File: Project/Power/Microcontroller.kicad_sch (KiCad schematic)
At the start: 11 parts, among them J13 I2C, J14 SWD, J15 SPI1, SW1 SW_Push, U14 STM32L422KBTx

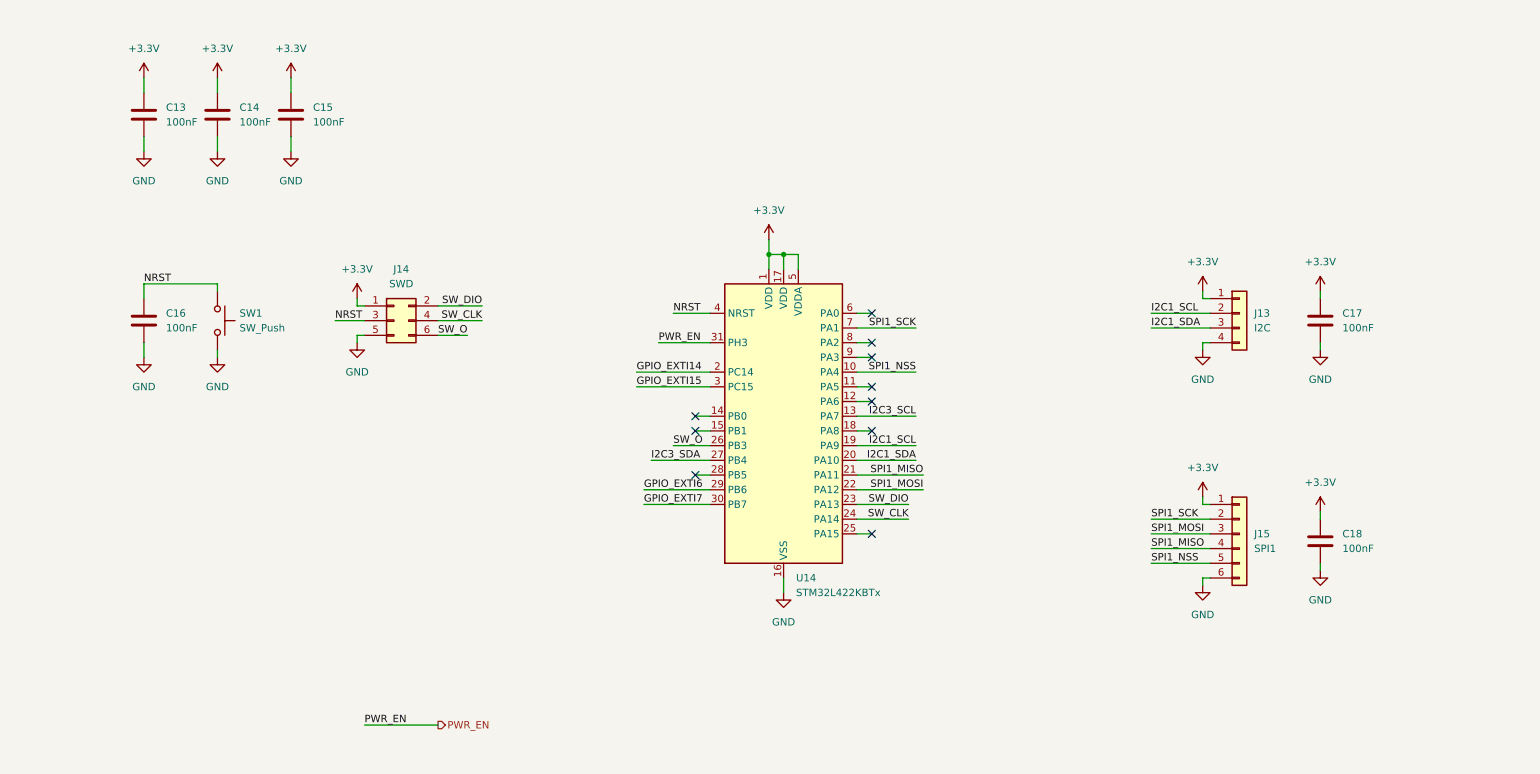
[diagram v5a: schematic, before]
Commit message: Change power microcontroller pin ordering
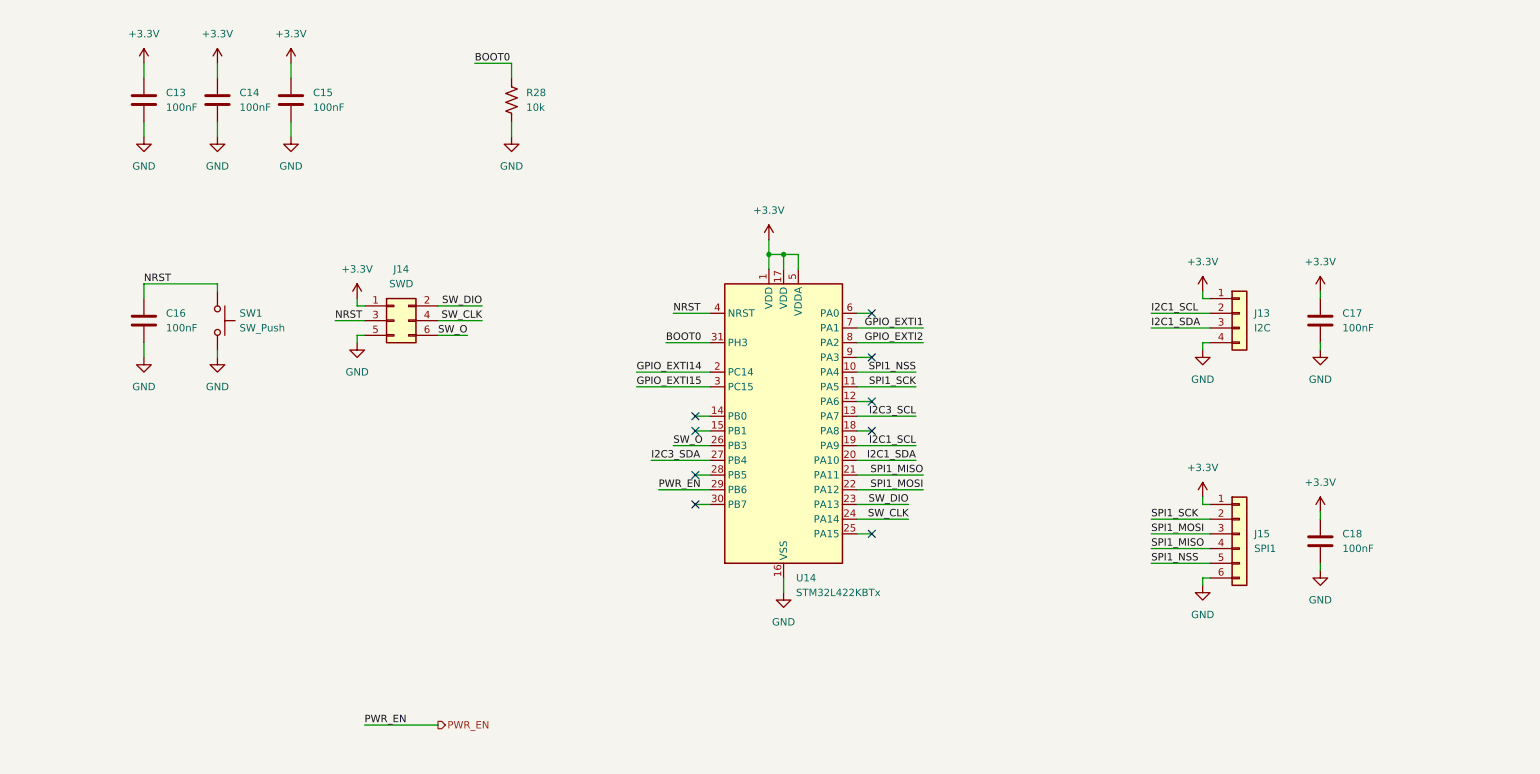
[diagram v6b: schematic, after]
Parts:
- added R28: 10k, Resistor_SMD:R_0603_1608Metric, symbol Device:R_US
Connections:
- net GPIO_EXTI6 is gone; now on net PWR_EN: U14.29 (PB6)
- net GND: now also R28.1
- net PWR_EN: no longer U14.31 (PH3)
- net SPI1_SCK: now also U14.11 (PA5); no longer U14.7 (PA1)
- net GPIO_EXTI2: now reaches U14.8 (PA2)
- net GPIO_EXTI7: no longer names the net of U14.30 (PB7)
- new net BOOT0: R28.2, U14.31 (PH3)
- new net GPIO_EXTI1: U14.7 (PA1)
- no-connect marks 10 -> 9
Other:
- moved on the sheet: C13, C14, C15

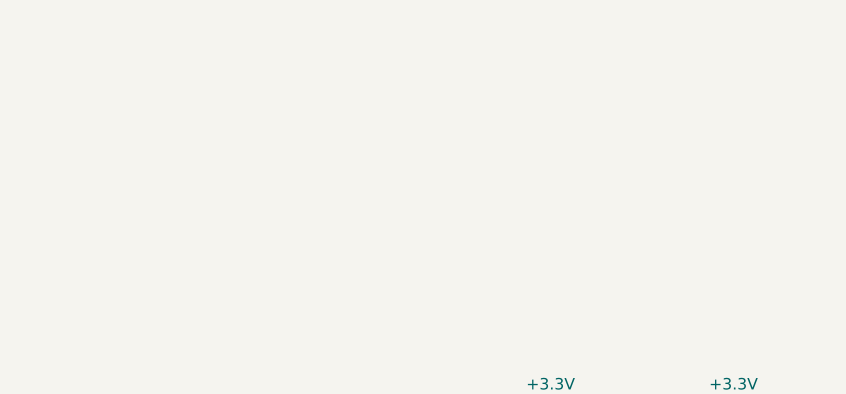
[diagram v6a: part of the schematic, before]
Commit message: Add I2C pull-up resistors
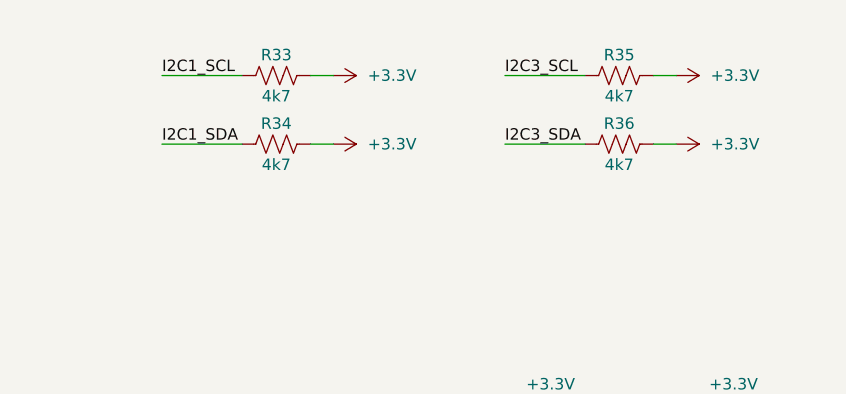
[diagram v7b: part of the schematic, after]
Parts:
- added R33, R34, R35, R36: 4k7, Resistor_SMD:R_0603_1608Metric, symbol Device:R_US
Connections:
- net +3.3V: now also R33.1, R34.1, R35.1, R36.1
- net I2C1_SCL: now also R33.2
- net I2C1_SDA: now also R34.2
- net I2C3_SCL: now also R35.2
- net I2C3_SDA: now also R36.2

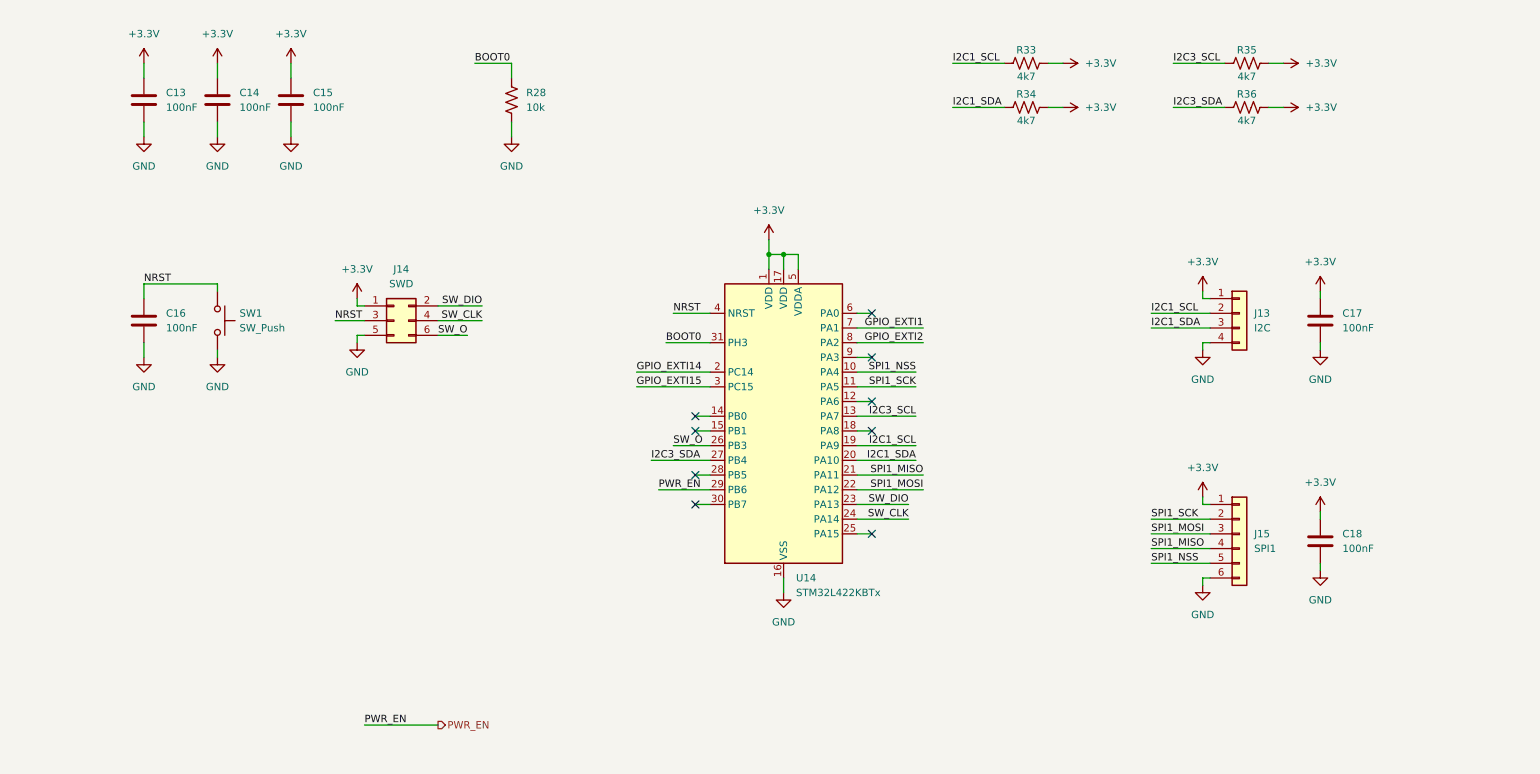
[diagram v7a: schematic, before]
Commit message: Add INA226 sensors for batteries
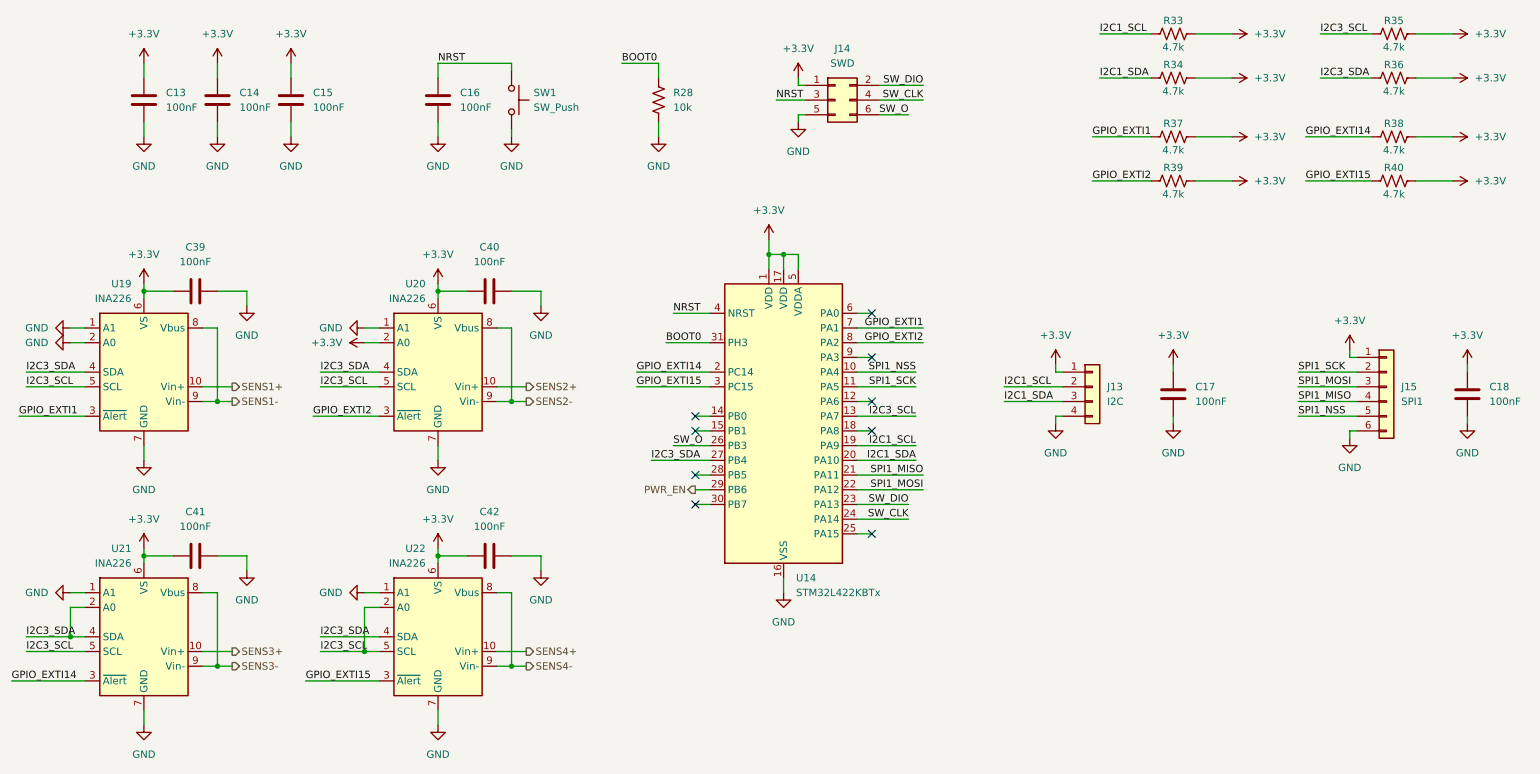
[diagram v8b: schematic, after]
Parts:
- added C39, C40, C41, C42: 100nF, Capacitor_SMD:C_0603_1608Metric, symbol Device:C
- added R37, R38, R39, R40: 4.7k, Resistor_SMD:R_0603_1608Metric, symbol Device:R_US
- added U19, U20, U21, U22: INA226, Package_SO:VSSOP-10_3x3mm_P0.5mm, symbol Sensor_Energy:INA226
- R33, R34, R35, R36: value 4k7 -> 4.7k
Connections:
- net +3.3V: now also C39.1, C40.1, C41.1, C42.1, R37.1, R38.1, R39.1, R40.1, U19.6 (VS), U20.2 (A0), U20.6 (VS), U21.6 (VS), U22.6 (VS)
- net GND: now also C39.2, C40.2, C41.2, C42.2, U19.1 (A1), U19.2 (A0), U19.7 (GND), U20.1 (A1), U20.7 (GND), U21.1 (A1), U21.7 (GND), U22.1 (A1), U22.7 (GND)
- net GPIO_EXTI1: now also R37.2, U19.3 (~{Alert})
- net GPIO_EXTI14: now also R38.2, U21.3 (~{Alert})
- net GPIO_EXTI15: now also R40.2, U22.3 (~{Alert})
- net GPIO_EXTI2: now also R39.2, U20.3 (~{Alert})
- net I2C3_SCL: now also U19.5 (SCL), U20.5 (SCL), U21.5 (SCL), U22.2 (A0), U22.5 (SCL)
- net I2C3_SDA: now also U19.4 (SDA), U20.4 (SDA), U21.2 (A0), U21.4 (SDA), U22.4 (SDA)
- new net SENS1+: U19.10 (Vin+)
- new net SENS1-: U19.8 (Vbus), U19.9 (Vin-)
- new net SENS2+: U20.10 (Vin+)
- new net SENS2-: U20.8 (Vbus), U20.9 (Vin-)
- new net SENS3+: U21.10 (Vin+)
- new net SENS3-: U21.8 (Vbus), U21.9 (Vin-)
- new net SENS4+: U22.10 (Vin+)
- new net SENS4-: U22.8 (Vbus), U22.9 (Vin-)
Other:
- moved on the sheet: C16, C17, C18, J13, J14, J15, R28, R33, R34, R35, R36, SW1
